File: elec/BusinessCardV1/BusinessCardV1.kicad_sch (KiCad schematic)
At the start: 0 parts

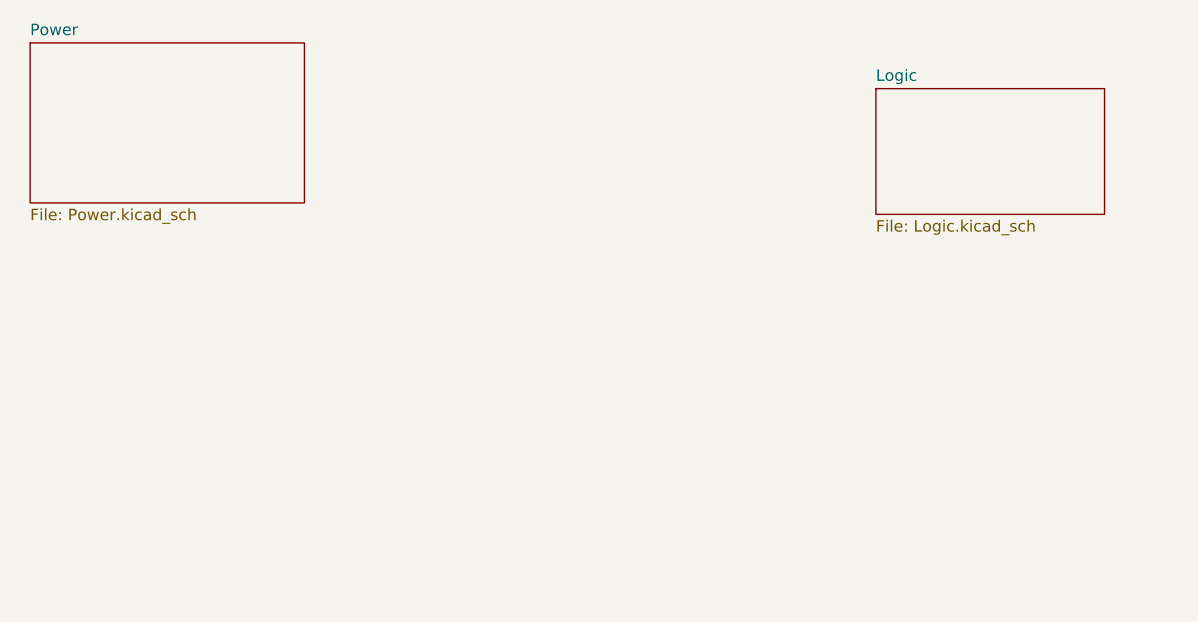
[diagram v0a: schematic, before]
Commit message: Started the power management
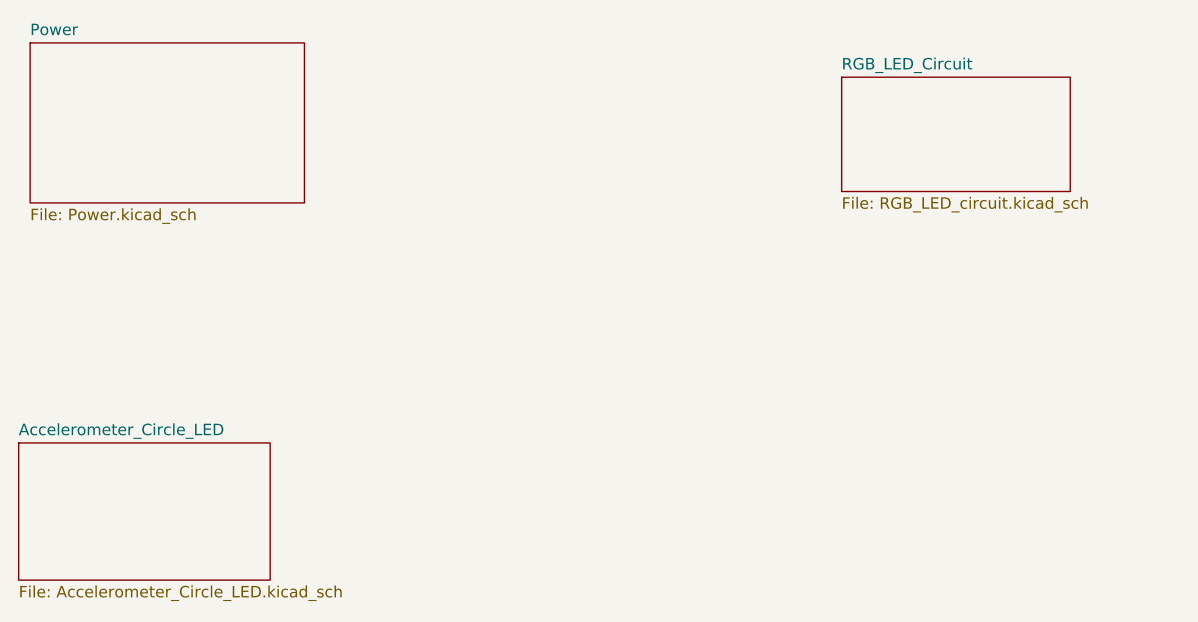
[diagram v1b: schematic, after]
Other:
- removed sheet Logic
- added sheet Accelerometer_Circle_LED (Accelerometer_Circle_LED.kicad_sch)
- added sheet RGB_LED_Circuit (RGB_LED_circuit.kicad_sch)
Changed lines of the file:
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@@
 	(paper "A4")
 	(sheet
-		(at 142.24 43.18)
-		(size 25.4 13.97)
+		(at 138.43 41.91)
+		(size 25.4 12.7)
 		(exclude_from_sim no)
 		(in_bom yes)
@@
 			(color 0 0 0 0.0000)
 		)
-		(property "Sheetname" "Logic"
-			(at 142.24 42.4684 0)
+		(property "Sheetname" "RGB_LED_Circuit"
+			(at 138.43 41.1984 0)
 			(effects
 				(font
@@
 			)
 		)
-		(property "Sheetfile" "Logic.kicad_sch"
-			(at 142.24 57.7346 0)
+		(property "Sheetfile" "RGB_LED_circuit.kicad_sch"
+			(at 138.43 55.1946 0)
 			(effects
 				(font
@@
 				)
 			)
+		)
+	)
+	(sheet
+		(at 46.99 82.55)
+		(size 27.94 15.24)
+		(exclude_from_sim no)
+		(in_bom yes)
+		(on_board yes)
+		(dnp no)
+		(fields_autoplaced yes)
+		(stroke
+			(width 0.1524)
+			(type solid)
+		)
+		(fill
+			(color 0 0 0 0.0000)
+		)
+		(property "Sheetname" "Accelerometer_Circle_LED"
+			(at 46.99 81.8384 0)
+			(effects
+				(font
+					(size 1.27 1.27)
+				)
+				(justify left bottom)
+			)
+		)
+		(property "Sheetfile" "Accelerometer_Circle_LED.kicad_sch"
+			(at 46.99 98.3746 0)
+			(effects
+				(font
+					(size 1.27 1.27)
+				)
+				(justify left top)
+			)
+		)
+		(instances
+			(project "BusinessCardV1"
+				(path "/28a1e4b0-497b-455a-8c80-759850e7b173"
+					(page "4")
+				)
+			)

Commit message: heheheha
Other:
- added sheet Buttons (Buttons.kicad_sch)
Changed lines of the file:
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@@
 	(paper "A4")
+	(sheet
+		(at 139.7 81.28)
+		(size 27.94 20.32)
+		(exclude_from_sim no)
+		(in_bom yes)
+		(on_board yes)
+		(dnp no)
+		(fields_autoplaced yes)
+		(stroke
+			(width 0.1524)
+			(type solid)
+		)
+		(fill
+			(color 0 0 0 0.0000)
+		)
+		(property "Sheetname" "Buttons"
+			(at 139.7 80.5684 0)
+			(effects
+				(font
+					(size 1.27 1.27)
+				)
+				(justify left bottom)
+			)
+		)
+		(property "Sheetfile" "Buttons.kicad_sch"
+			(at 139.7 102.1846 0)
+			(effects
+				(font
+					(size 1.27 1.27)
+				)
+				(justify left top)
+			)
+		)
+		(instances
+			(project "BusinessCardV1"
+				(path "/28a1e4b0-497b-455a-8c80-759850e7b173"
+					(page "5")
+				)
+			)
+		)
+	)
 	(sheet
 		(at 138.43 41.91)

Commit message: pew
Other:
- added sheet Accelerometer_Circle_Setup (Accelerometer_Circle_Setup.kicad_sch)
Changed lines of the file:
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@@
+		)
+	)
+	(sheet
+		(at 48.26 123.19)
+		(size 26.67 20.32)
+		(exclude_from_sim no)
+		(in_bom yes)
+		(on_board yes)
+		(dnp no)
+		(fields_autoplaced yes)
+		(stroke
+			(width 0.1524)
+			(type solid)
+		)
+		(fill
+			(color 0 0 0 0.0000)
+		)
+		(property "Sheetname" "Accelerometer_Circle_Setup"
+			(at 48.26 122.4784 0)
+			(effects
+				(font
+					(size 1.27 1.27)
+				)
+				(justify left bottom)
+			)
+		)
+		(property "Sheetfile" "Accelerometer_Circle_Setup.kicad_sch"
+			(at 48.26 144.0946 0)
+			(effects
+				(font
+					(size 1.27 1.27)
+				)
+				(justify left top)
+			)
+		)
+		(instances
+			(project "BusinessCardV1"
+				(path "/28a1e4b0-497b-455a-8c80-759850e7b173"
+					(page "6")
+				)
+			)
 		)
 	)

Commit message: PCB art
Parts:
- added U22: TPD12S520DBT, Package_SO:TSSOP-38_4.4x9.7mm_P0.5mm, symbol Interface_HDMI:TPD12S520DBT
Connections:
- new net: U22.10 (TMDS_D0+), U22.29 (TMDS_D0+)
- new net: U22.11 (TMDS_GND), U22.14 (TMDS_GND), U22.25 (TMDS_GND), U22.28 (TMDS_GND), U22.31 (TMDS_GND), U22.34 (TMDS_GND), U22.5 (TMDS_GND), U22.8 (TMDS_GND)
- new net: U22.12 (TMDS_D0-), U22.27 (TMDS_D0-)
- new net: U22.13 (TMDS_CK+), U22.26 (TMDS_CK+)
- new net: U22.15 (TMDS_CK-), U22.24 (TMDS_CK-)
- new net: U22.3 (GND), U22.36 (GND)
- new net: U22.30 (TMDS_D1-), U22.9 (TMDS_D1-)
- new net: U22.32 (TMDS_D1+), U22.7 (TMDS_D1+)
- new net: U22.33 (TMDS_D2-), U22.6 (TMDS_D2-)
- new net: U22.35 (TMDS_D2+), U22.4 (TMDS_D2+)
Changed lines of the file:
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@@
 	(generator_version "9.0")
 	(paper "A4")
+	(symbol
+		(lib_id "Interface_HDMI:TPD12S520DBT")
+		(at 240.03 50.8 0)
+		(unit 1)
+		(exclude_from_sim no)
+		(in_bom yes)
+		(on_board yes)
+		(dnp no)
+		(fields_autoplaced yes)
+		(property "Reference" "U22"
+			(at 244.7133 20.32 0)
+			(effects
+				(font
+					(size 1.27 1.27)
+				)
+				(justify left)
+			)
+		)
+		(property "Value" "TPD12S520DBT"
+			(at 244.7133 22.86 0)
+			(effects
+				(font
+					(size 1.27 1.27)
+				)
+				(justify left)
+			)
+		)
+		(property "Footprint" "Package_SO:TSSOP-38_4.4x9.7mm_P0.5mm"
+			(at 236.22 57.15 0)
+			(effects
+				(font
+					(size 1.27 1.27)
+				)
+				(hide yes)
+			)
+		)
+		(property "Datasheet" "http://www.ti.com/lit/ds/symlink/tpd12s520.pdf"
+			(at 236.22 57.15 0)
+			(effects
+				(font
+					(size 1.27 1.27)
+				)
+				(hide yes)
+			)
+		)
+		(property "Description" "HDMI Receiver Port Protection and Interface Device, TSSOP-38"
+			(at 240.03 50.8 0)
+			(effects
+				(font
+					(size 1.27 1.27)
+				)
+				(hide yes)
+			)
+		)
+		(pin "33"
+		)
+		(pin "30"
+		)
+		(pin "27"
+		)
+		(pin "24"
+		)
+		(pin "18"
+		)
+		(pin "9"
+		)
+		(pin "29"
+		)
+		(pin "12"
+		)
+		(pin "6"
+		)
+		(pin "4"
+		)
+		(pin "15"
+		)
+		(pin "35"
+		)
+		(pin "13"
+		)
+		(pin "32"
+		)
+		(pin "7"
+		)
+		(pin "10"
+		)
+		(pin "26"
+		)
+		(pin "16"
+		)
+		(pin "17"
+		)
+		(pin "3"
+		)
+		(pin "2"
+		)
+		(pin "14"
+		)
+		(pin "22"
+		)
+		(pin "8"
+		)
+		(pin "11"
+		)
+		(pin "25"
+		)
+		(pin "20"
+		)
+		(pin "34"
+		)
+		(pin "1"
+		)
+		(pin "36"
+		)
+		(pin "37"
+		)
+		(pin "31"
+		)
+		(pin "28"
+		)
+		(pin "5"
+		)
+		(pin "23"
+		)
+		(pin "38"
+		)
+		(pin "19"
+		)
+		(pin "21"
+		)
+		(instances
+			(project ""
+				(path "/28a1e4b0-497b-455a-8c80-759850e7b173"
+					(reference "U22")
+					(unit 1)
+				)
+			)
+		)
+	)
 	(sheet
 		(at 139.7 81.28)

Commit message: Missing update
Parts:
- U22: footprint Package_SO:TSSOP-38_4.4x9.7mm_P0.5mm -> PCBArt:pcbart
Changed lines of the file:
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@@
 			)
 		)
-		(property "Footprint" "Package_SO:TSSOP-38_4.4x9.7mm_P0.5mm"
+		(property "Footprint" "PCBArt:pcbart"
 			(at 236.22 57.15 0)
 			(effects

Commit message: Position made, but kicad lagging everytime i add a wire
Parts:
- U22: footprint PCBArt:pcbart -> PCBArt:design
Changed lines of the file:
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@@
 			)
 		)
-		(property "Footprint" "PCBArt:pcbart"
+		(property "Footprint" "PCBArt:design"
 			(at 236.22 57.15 0)
 			(effects

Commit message: PCB routed
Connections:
- no-connect marks 0 -> 21
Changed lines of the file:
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@@
 	(generator_version "9.0")
 	(paper "A4")
+	(no_connect
+		(at 260.35 55.88)
+	)
+	(no_connect
+		(at 219.71 58.42)
+	)
+	(no_connect
+		(at 242.57 22.86)
+	)
+	(no_connect
+		(at 242.57 78.74)
+	)
+	(no_connect
+		(at 219.71 45.72)
+	)
+	(no_connect
+		(at 237.49 78.74)
+	)
+	(no_connect
+		(at 219.71 50.8)
+	)
+	(no_connect
+		(at 219.71 40.64)
+	)
+	(no_connect
+		(at 219.71 63.5)
+	)
+	(no_connect
+		(at 219.71 33.02)
+	)
+	(no_connect
+		(at 260.35 58.42)
+	)
+	(no_connect
+		(at 219.71 30.48)
+	)
+	(no_connect
+		(at 260.35 50.8)
+	)
+	(no_connect
+		(at 237.49 22.86)
+	)
+	(no_connect
+		(at 219.71 35.56)
+	)
+	(no_connect
+		(at 219.71 43.18)
+	)
+	(no_connect
+		(at 219.71 27.94)
+	)
+	(no_connect
+		(at 219.71 55.88)
+	)
+	(no_connect
+		(at 260.35 27.94)
+	)
+	(no_connect
+		(at 260.35 63.5)
+	)
+	(no_connect
+		(at 219.71 38.1)
+	)
 	(symbol
 		(lib_id "Interface_HDMI:TPD12S520DBT")
